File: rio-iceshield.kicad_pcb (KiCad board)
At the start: 2 copper layers, 87.6 x 56 mm, 94 parts, among them J2 Conn_01x06, J3 Conn_01x06, J4 Conn_01x06, J5 Conn_01x06, J6 Conn_01x06, J7 Conn_02x06_Odd_Even, U1 ICE40UP5K-SG48ITR, U10 PC817, U11 PC817, U12 PC817, U13 PC817, U14 PC817, U2 AT25SF041B-SHD 4 Mb, U3 LD3985M122R_SOT23, U4 ULN2803A, U5 ULN2803A, U7 PC817, U8 PC817, U9 PC817, X2 XO91, j1 GPIO

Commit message: WIP
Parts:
- C1, C10, C11, C12, C13, C14, C15, C16, C17, C18, C2, C3, C5, C6, C7, C8, C9: footprint Capacitor_SMD:C_0805_2012Metric_Pad1.18x1.45mm_HandSolder -> Capacitor_SMD:C_0603_1608Metric_Pad1.08x0.95mm_HandSolder
- C4: footprint Capacitor_SMD:C_0805_2012Metric_Pad1.18x1.45mm_HandSolder -> Capacitor_SMD:C_0603_1608Metric_Pad1.08x0.95mm_HandSolder; moved to F.Cu
- D1: value 1N 4148WT7 DII -> 1N4148WS; footprint Diode_SMD:D_0603_1608Metric -> Diode_SMD:D_SOD-123
- R1, R13, R14, R15, R16, R17, R18, R19, R20, R21, R22, R23, R24, R25, R26, R27, R31, R32: footprint Resistor_SMD:R_0805_2012Metric_Pad1.20x1.40mm_HandSolder -> Resistor_SMD:R_0603_1608Metric_Pad0.98x0.95mm_HandSolder
- R10, R11: value 900 -> 1k; footprint Resistor_SMD:R_0805_2012Metric_Pad1.20x1.40mm_HandSolder -> Resistor_SMD:R_0603_1608Metric_Pad0.98x0.95mm_HandSolder
- R12: footprint Resistor_SMD:R_0805_2012Metric_Pad1.20x1.40mm_HandSolder -> Resistor_SMD:R_0603_1608Metric_Pad0.98x0.95mm_HandSolder; moved to F.Cu
- R2, R28, R29, R3, R30, R4, R5, R6, R7, R9: footprint Resistor_SMD:R_1206_3216Metric -> Resistor_SMD:R_0603_1608Metric_Pad0.98x0.95mm_HandSolder
- R8: footprint Resistor_SMD:R_1206_3216Metric -> Resistor_SMD:R_0603_1608Metric_Pad0.98x0.95mm_HandSolder; moved to F.Cu
- U10, U11, U12, U13, U14, U7, U8, U9: footprint Package_DIP:DIP-4_W7.62mm -> Package_SO:SOP-4_4.4x2.6mm_P1.27mm
- U4, U5: footprint Package_SO:SOIC-18W_7.5x11.6mm_P1.27mm -> Package_SO:SOP-18_7.495x11.515mm_P1.27mm
- moved U8 4.11 mm to (112.7, 64.6)
- moved U7 4.10 mm to (105.7, 64.6)
- moved R8 3.93 mm to (144.1, 67.5)
- moved U10 3.84 mm to (126.7, 64.9)
- moved U11 3.76 mm to (133.7, 65.0)
- moved U9 3.72 mm to (119.5, 65.0)
- moved U12 3.68 mm to (140.5, 65.0)
- moved U13 3.67 mm to (147.6, 65.1)
- moved U14 3.50 mm to (154.5, 65.2)
- moved R12 0.24 mm to (166.5, 47.5)
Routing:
- net gnd: track 304.3 -> 0.00 mm, vias 19 -> 0
- net 42: track 36.5 -> 34.0 mm
- net in_power: track 161.8 -> 159.4 mm
- net Net-(R8-Pad1): track 4.38 -> 2.31 mm
- net 3v3: track 238.6 -> 239.2 mm
- net SPI_CS1: track 76.7 -> 76.9 mm, vias 1 -> 0
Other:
- copper layers 2 -> 4

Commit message: wip
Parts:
- C10, C11, C12, C13, C14, C15, C16, C17, C18, C5, C6, C7, C8, C9, D1, R1, R13, R14, R15, R16, R17, R18, R19, R2, R20, R21, R22, R23, R24, R25, R26, R27, R28, R29, R3, R30, R4, R5, R6, R7, R9: moved to F.Cu
- moved R12 33.8 mm to (133.8, 55.9)
- moved C4 32.9 mm to (147.7, 55.2)
- moved U2 32.9 mm to (141.4, 55.2)
- moved C3 23.8 mm to (129.3, 57.1)
- moved C2 23.8 mm to (126.8, 57.1)
- moved D2 23.5 mm to (180.8, 60.9)
- moved D3 23.5 mm to (184.3, 60.9)
- moved R10 23.2 mm to (183.0, 56.3)
- moved R11 23.2 mm to (180.5, 56.3)
- moved C7 20.1 mm to (167.7, 60.0), turned to -90 degrees
- moved C14 19.8 mm to (177.0, 64.4), turned to -90 degrees
- moved C1 18.4 mm to (126.1, 53.2)
- moved U3 18.4 mm to (129.2, 53.1)
- moved C17 18.0 mm to (173.8, 64.4), turned to -90 degrees
- moved C6 17.1 mm to (185.1, 52.4), turned to 0 degrees
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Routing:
- net 3v3: track 239.2 -> 0.00 mm, vias 12 -> 0
- net in_power: track 159.4 -> 0.00 mm
- net 12v: track 109.7 -> 0.00 mm, vias 4 -> 0
- net 5v: track 105.7 -> 0.00 mm, vias 2 -> 0
- net 1v2: track 92.0 -> 0.00 mm, vias 3 -> 0
- net SPI_MOSI: track 86.5 -> 0.00 mm, vias 1 -> 0
- net SPI_SCK: track 81.2 -> 0.00 mm, vias 1 -> 0
- net 41: track 80.1 -> 0.00 mm
- net SPI_MISO: track 77.2 -> 0.00 mm
- net SPI_CS1: track 76.9 -> 0.00 mm
- net 40: track 72.9 -> 0.00 mm
- net CRESET: track 70.3 -> 0.00 mm, vias 2 -> 0
- net out1: track 67.4 -> 0.00 mm
- net 39: track 65.2 -> 0.00 mm
- net out2: track 62.0 -> 0.00 mm, vias 1 -> 0
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
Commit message: wip
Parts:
- moved R9 14.5 mm to (160.7, 60.7)
- moved R7 11.5 mm to (146.4, 66.4), turned to 90 degrees
- moved R5 11.0 mm to (133.1, 66.8)
- moved R29 8.75 mm to (102.6, 66.6), turned to -90 degrees
- moved U13 8.10 mm to (152.9, 62.3), turned to 0 degrees
- moved U11 7.51 mm to (139.4, 62.2), turned to 0 degrees
- moved U7 7.49 mm to (113.5, 62.3), turned to 0 degrees
- moved U9 7.42 mm to (126.4, 62.4), turned to 0 degrees
- moved R8 7.29 mm to (146.5, 62.3)
- moved R6 7.05 mm to (133.0, 62.0)
- moved R2 6.63 mm to (106.8, 62.2)
- moved R28 4.24 mm to (120.0, 62.1)
- moved R4 4.24 mm to (120.0, 67.4)
- moved R3 3.49 mm to (106.7, 66.6)
- moved U8 2.18 mm to (113.5, 66.8), turned to 180 degrees
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
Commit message: wip
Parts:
- removed J7: Conn_02x06_Odd_Even, Connector_PinHeader_2.54mm:PinHeader_2x06_P2.54mm_Vertical
- added TP10: TestPoint_Small, TestPoint:TestPoint_Pad_2.0x2.0mm, B.Cu at (167.6, 45.8)
- added TP11: TestPoint_Small, TestPoint:TestPoint_Pad_2.0x2.0mm, F.Cu at (154.0, 53.0)
- added TP12: TestPoint_Small, TestPoint:TestPoint_Pad_2.0x2.0mm, F.Cu at (157.0, 53.0)
- added TP13: TestPoint_Small, TestPoint:TestPoint_Pad_2.0x2.0mm, F.Cu at (157.0, 56.0)
- added TP2: TestPoint_Small, TestPoint:TestPoint_Pad_2.0x2.0mm, B.Cu at (184.2, 49.0)
- added TP3: TestPoint_Small, TestPoint:TestPoint_Pad_2.0x2.0mm, B.Cu at (173.1, 54.8)
- added TP4: TestPoint_Small, TestPoint:TestPoint_Pad_2.0x2.0mm, B.Cu at (184.8, 52.7)
- added TP5: TestPoint_Small, TestPoint:TestPoint_Pad_2.0x2.0mm, B.Cu at (184.9, 57.2)
- added TP6: TestPoint_Small, TestPoint:TestPoint_Pad_2.0x2.0mm, B.Cu at (177.2, 56.8)
- added TP7: TestPoint_Small, TestPoint:TestPoint_Pad_2.0x2.0mm, B.Cu at (173.5, 59.5)
- added TP8: TestPoint_Small, TestPoint:TestPoint_Pad_2.0x2.0mm, B.Cu at (179.0, 62.0)
- added TP9: TestPoint_Small, TestPoint:TestPoint_Pad_2.0x2.0mm, F.Cu at (154.0, 56.0)
- JP1, R31, R32: moved to F.Cu
- moved R32 27.7 mm to (103.0, 62.8), turned to -90 degrees
- moved R31 22.1 mm to (103.1, 66.5)
- moved C6 16.8 mm to (168.5, 49.9), turned to -90 degrees
- moved C7 10.3 mm to (165.9, 49.9)
- moved R9 10.2 mm to (158.1, 70.6)
- moved R28 7.84 mm to (126.8, 58.2), turned to 0 degrees
- moved C3 5.08 mm to (132.6, 53.2)
- moved C15 5.05 mm to (173.3, 46.2), turned to 180 degrees
- moved C13 4.28 mm to (173.3, 50.4), turned to 180 degrees
- moved C2 3.88 mm to (130.6, 56.3), turned to 0 degrees
- moved C12 3.62 mm to (173.9, 66.1), turned to 0 degrees
- moved C14 3.45 mm to (173.9, 63.0), turned to 0 degrees
- moved R11 2.54 mm to (183.0, 56.3)
- moved R29 2.20 mm to (104.8, 66.5)
- moved R30 2.10 mm to (104.8, 62.2), turned to 90 degrees
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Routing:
- net gnd: track 0.00 -> 172.6 mm, vias 0 -> 30
- net out1: track 0.00 -> 120.3 mm, vias 0 -> 2
- net 12v: track 0.00 -> 116.9 mm
- net in_power: track 0.00 -> 112.2 mm
- net 1v2: track 0.00 -> 109.4 mm, vias 0 -> 3
- net 5v: track 0.00 -> 109.4 mm
- net out2: track 0.00 -> 104.4 mm
- net j1_step: track 0.00 -> 98.6 mm, vias 0 -> 2
- net j1_dir: track 0.00 -> 87.4 mm, vias 0 -> 1
- net 40: track 0.00 -> 81.2 mm, vias 0 -> 4
- net SPI_CS1: track 0.00 -> 76.6 mm, vias 0 -> 2
- net 41: track 0.00 -> 75.1 mm, vias 0 -> 5
- net enable: track 0.00 -> 73.7 mm, vias 0 -> 1
- net j2_step: track 0.00 -> 67.8 mm, vias 0 -> 1
- net SPI_MOSI: track 0.00 -> 61.8 mm, vias 0 -> 2
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- added copper zone on In2.Cu, net 3v3
- added copper zone on In1.Cu, net gnd
- removed copper zone on B.Cu, net 5v
- removed copper zone on F.Cu, net gnd

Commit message: wip
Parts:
- removed JP1, JP2: SolderJumper_3_Open, Jumper:SolderJumper-3_P1.3mm_Open_Pad1.0x1.5mm
- removed TP10, TP11, TP12, TP13, TP2, TP3, TP4, TP5, TP6, TP7, TP8, TP9: TestPoint_Small, TestPoint:TestPoint_Pad_2.0x2.0mm
- removed U10, U11, U12, U13, U14, U8, U9: PC817, Package_SO:SOP-4_4.4x2.6mm_P1.27mm
- removed U3: LD3985M122R_SOT23, Package_TO_SOT_SMD:SOT-23-5
- removed X2: XO91, Oscillator:Oscillator_SMD_EuroQuartz_XO91-4Pin_7.0x5.0mm
- added C19: 100n, Capacitor_SMD:C_0603_1608Metric_Pad1.08x0.95mm_HandSolder, F.Cu at (113.5, 63.8)
- added C20: 100n, Capacitor_SMD:C_0603_1608Metric_Pad1.08x0.95mm_HandSolder, F.Cu at (113.2, 70.9)
- added C21: 100n, Capacitor_SMD:C_0603_1608Metric_Pad1.08x0.95mm_HandSolder, F.Cu at (113.6, 77.8)
- added C22: 100n, Capacitor_SMD:C_0603_1608Metric_Pad1.08x0.95mm_HandSolder, F.Cu at (113.3, 80.4)
- added C23: 100n, Capacitor_SMD:C_0603_1608Metric_Pad1.08x0.95mm_HandSolder, F.Cu at (118.0, 87.4)
- added C24: 100n, Capacitor_SMD:C_0603_1608Metric_Pad1.08x0.95mm_HandSolder, F.Cu at (127.8, 80.5)
- added C25: 100n, Capacitor_SMD:C_0603_1608Metric_Pad1.08x0.95mm_HandSolder, F.Cu at (127.7, 87.4)
- added R33: 1k2, Resistor_SMD:R_0603_1608Metric_Pad0.98x0.95mm_HandSolder, F.Cu at (122.5, 57.5)
- added R34: 1k2, Resistor_SMD:R_0603_1608Metric_Pad0.98x0.95mm_HandSolder, F.Cu at (127.1, 54.1)
- added R35: 1k2, Resistor_SMD:R_0603_1608Metric_Pad0.98x0.95mm_HandSolder, F.Cu at (125.5, 54.1)
- added R36: 1k2, Resistor_SMD:R_0603_1608Metric_Pad0.98x0.95mm_HandSolder, F.Cu at (122.5, 54.3)
- added R37: 1k2, Resistor_SMD:R_0603_1608Metric_Pad0.98x0.95mm_HandSolder, F.Cu at (122.5, 55.9)
- added U15: ELM453-TA-V, Package_SO:MFSOP6-5_4.4x3.6mm_P1.27mm, F.Cu at (116.0, 60.8)
- added U16: ELM453-TA-V, Package_SO:MFSOP6-5_4.4x3.6mm_P1.27mm, F.Cu at (115.7, 67.9)
- added U17: ELM453-TA-V, Package_SO:MFSOP6-5_4.4x3.6mm_P1.27mm, F.Cu at (115.8, 74.7)
- added U18: ELM453-TA-V, Package_SO:MFSOP6-5_4.4x3.6mm_P1.27mm, F.Cu at (115.7, 83.5)
- added U19: ELM453-TA-V, Package_SO:MFSOP6-5_4.4x3.6mm_P1.27mm, F.Cu at (115.8, 90.4)
- added U20: ELM453-TA-V, Package_SO:MFSOP6-5_4.4x3.6mm_P1.27mm, F.Cu at (125.3, 83.5)
- added U21: ELM453-TA-V, Package_SO:MFSOP6-5_4.4x3.6mm_P1.27mm, F.Cu at (125.4, 90.5)
- added U6: ELM453-TA-V, Package_SO:MFSOP6-5_4.4x3.6mm_P1.27mm, F.Cu at (116.0, 53.8)
- D1: footprint Diode_SMD:D_SOD-123 -> Diode_SMD:D_SOD-323_HandSoldering
- U2: footprint Package_SO:SOIC-8W_5.3x5.3mm_P1.27mm -> Package_SO:SOIC-8_3.9x4.9mm_P1.27mm
- U7: value PC817 -> LM317LD13TR; footprint Package_SO:SOP-4_4.4x2.6mm_P1.27mm -> Package_SO:SOIC-8_3.9x4.9mm_P1.27mm
- moved J3 69.1 mm to (182.0, 48.5), turned to 180 degrees
- moved Jo1 63.5 mm to (175.4, 68.8)
- moved R1 52.9 mm to (129.8, 69.7), turned to 90 degrees
- moved J4 52.0 mm to (183.3, 68.9)
- moved R31 50.6 mm to (144.5, 95.6), turned to -90 degrees
- moved J2 50.5 mm to (175.3, 88.9)
- moved C11 50.2 mm to (131.4, 69.7), turned to -90 degrees
- moved C16 50.1 mm to (129.7, 73.5), turned to -90 degrees
- moved C15 48.6 mm to (133.0, 73.5), turned to -90 degrees
- moved R32 48.3 mm to (144.5, 87.6)
- moved C8 47.8 mm to (133.0, 69.7), turned to -90 degrees
- moved C13 47.8 mm to (131.4, 73.5), turned to -90 degrees
- moved C10 47.2 mm to (135.5, 64.1), turned to -90 degrees
- moved C9 46.8 mm to (137.1, 64.1), turned to -90 degrees
- moved C5 46.4 mm to (133.3, 77.6)
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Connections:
- C1 pad 1: 3v3 -> 5v
- C2 pad 1: Net-(U3-BYP) -> 1v2
- U7 pad 1: Net-(R2-Pad1) -> 5v
- U7 pad 2: Net-(input1-Pin_1) -> 1v2
- U7 pad 3: gnd -> 1v2
- U7 pad 4: 41 -> gnd
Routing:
- net 5v: track 109.4 -> 235.5 mm, vias 0 -> 5
- net out1: track 120.3 -> 26.1 mm, vias 2 -> 1
- net out2: track 104.4 -> 22.3 mm
- net j1_step: track 98.6 -> 19.7 mm, vias 2 -> 0
- net j1_dir: track 87.4 -> 17.4 mm, vias 1 -> 0
- net 35: track 52.6 -> 0.00 mm, vias 3 -> 0
- net SPI_CS1: track 76.6 -> 29.7 mm, vias 2 -> 3
- net j3_dir: track 54.2 -> 8.44 mm, vias 1 -> 0
- net j3_step: track 55.8 -> 13.7 mm, vias 1 -> 0
- net 13: track 57.4 -> 17.4 mm
- net j5_step: track 55.0 -> 20.4 mm
- net SPI_SCK: track 61.4 -> 27.5 mm
- net SPI_MISO: track 61.2 -> 28.4 mm, vias 4 -> 3
- net j2_step: track 67.8 -> 35.8 mm
- net in_power: track 112.2 -> 141.8 mm, vias 0 -> 5
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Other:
- board text added: "rio-iceshield-v2 https://github.com/digiexchris/rio-iceshield-v2 based on rio-iceshield https://github.com/multigcs/rio-iceshield"

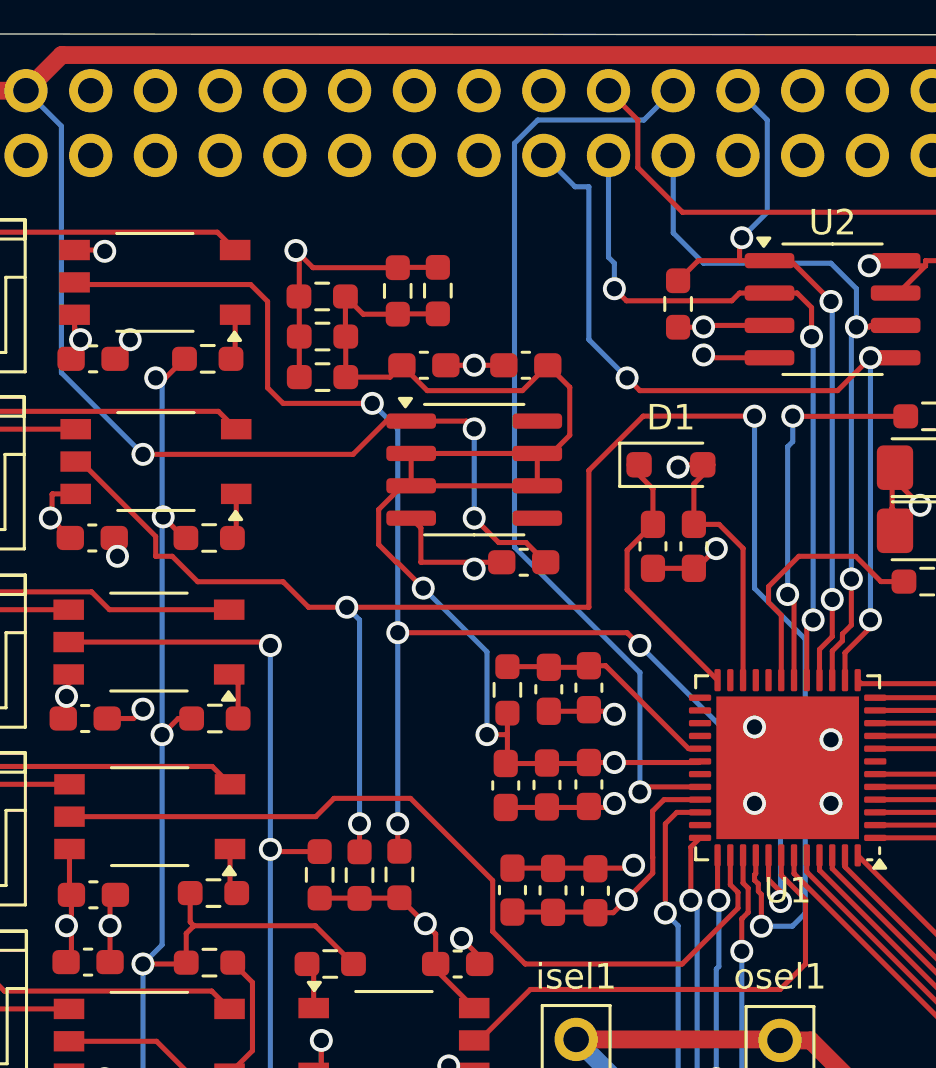
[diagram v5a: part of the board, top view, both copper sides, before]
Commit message: Fix missing clk line
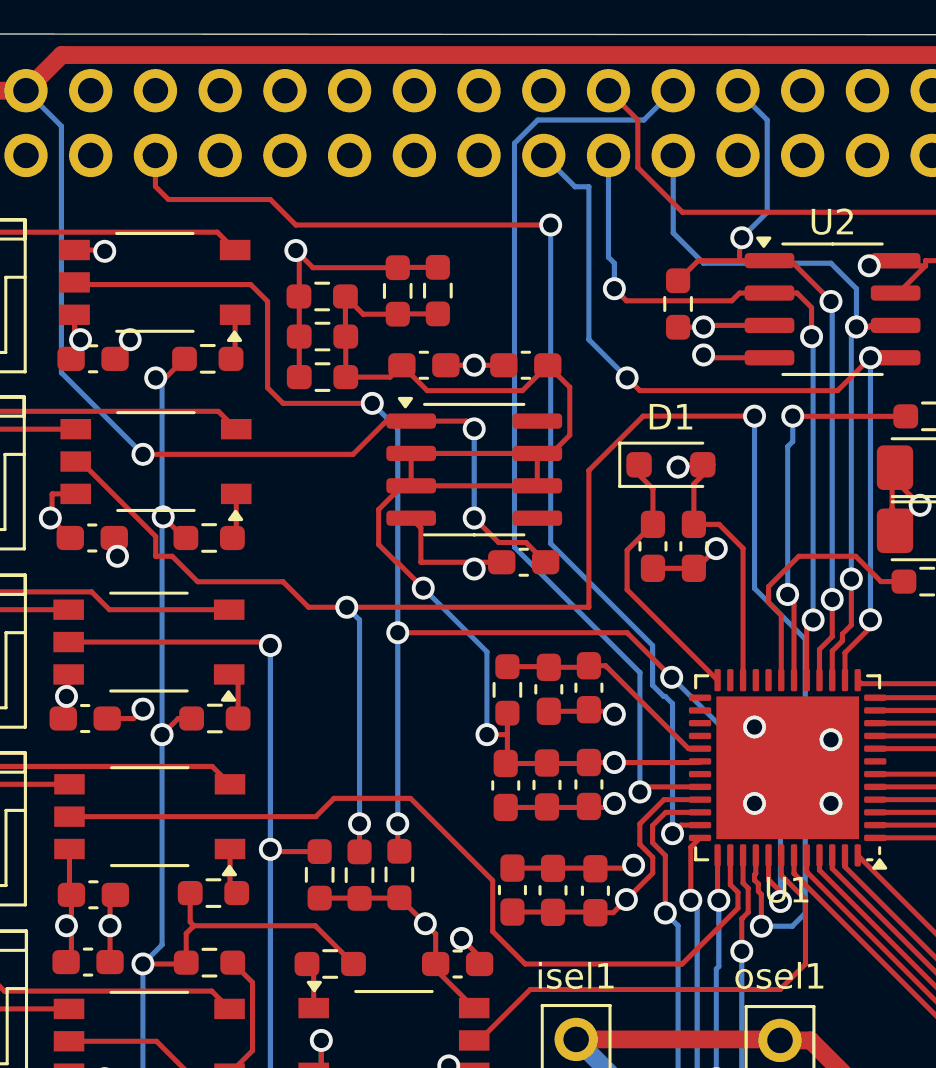
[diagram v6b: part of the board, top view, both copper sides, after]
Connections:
- j1 pad 7: RPI_CLK -> 35
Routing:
- net 35: track 0.00 -> 44.5 mm, vias 0 -> 2
- net 34: track 25.2 -> 25.9 mm

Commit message: Documentation update
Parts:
- added G***: LOGO, rio-solidwater-shield:qrcode-13.9x13.9, B.Cu at (160.5, 56.0)
- moved J2 1.36 mm to (173.9, 88.9)
- moved Jo1 1.36 mm to (174.0, 68.8)
- renumbered +24V-1 to EXT
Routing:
- net j2_dir: track 32.8 -> 50.1 mm
- net j2_step: track 35.8 -> 50.3 mm
- net enable: track 79.8 -> 84.6 mm
- net 5v: track 235.5 -> 238.2 mm
- net j1_step: track 19.7 -> 18.3 mm
- net j1_dir: track 17.4 -> 16.0 mm
- net 12v: track 125.9 -> 127.3 mm
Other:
- board text added: "+ 5-50v -"
- board text added: "EXT 5v"
- board text added: "I1: G + S"
- board text added: "I2: G + S"
- board text added: "I3: G + S"
- board text added: "I4: G + S"
- board text added: "I5: G + S"
- board text added: "I6: G + S"
- board text added: "I7: G + S"
- board text added: "I8: G + S"
- board text added: "O1: G + S"
- board text added: "O2: G + S"
- board text added: "S + -"
- board text added: "S1: D S E 5v G EXT"
- board text added: "S2: D S E 5v G EXT"
- board text added: "S3: D S E 5v G EXT"
- board text added: "S4: D S E 5v G EXT"
- board text added: "S5: D S E 5v G EXT"
- board text added: "S6: D S E 5v G EXT"
- board text added: "rio-solidwater-shield"
- board text removed: "rio-iceshield-v2 https://github.com/digiexchris/rio-iceshield-v2 based on rio-iceshield https://github.com/multigcs/rio-iceshield"
